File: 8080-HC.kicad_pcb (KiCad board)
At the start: 4 copper layers, 354 parts, among them U1 74HCU04, U10 74HC00, U11 74HC126, U12 74HC161, U13 74HC238, U14 74HC238, U15 74HC238, U16 74HC238, U17 74HC04, U178 74LS03, U18 74HC05, U180 74HC244, U181 74HC244, U182 74HC244, U19 74HC74, U193 74HC244, U194 74HC244, U195 74HC244, U2 74HC74, U20 74HC373, U21 74HC373, U214 74HC373, U215 74HC193, U216 74HC193, U217 74HC193, U218 74HC193, U22 74HC373, U227 74HC04, U228 74HC04, U229 74HC04, U23 74HC373, U230 74HC04, U231 74HC245, U232 74HC04, U233 74HC04, U234 74LS373, U239 74HC74, U24 74HC373, U242 74HC00, U243 74HCU04, U244 74HC00, U25 74HC244, U26 74HC244, U27 74HC244, U28 74HC244, U29 74HC244, U3 74HC00, U30 74HC373, U31 74HC373, U32 74HC244, U33 74HC244, U34 74HC244, U35 74HC244, U36 74HC373, U38 74HC244, U39 74HC244, U4 74HC04, U48 74HC04, U49 74HC04, U5 74HC00, U50 74HC04, U51 74HC04, U52 74HC04, U53 74HC238, U54 74HC238, U55 74HC238, U56 74HC238, U57 74HC04, U58 74HC04, U6 74HC04, U69 74HC05, U7 74HC05, U70 74LS05, U71 74HC04, U72 74LS126, U73 74LS126, U74 74LS126, U75 74LS126, U76 74LS126, U77 74HC00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

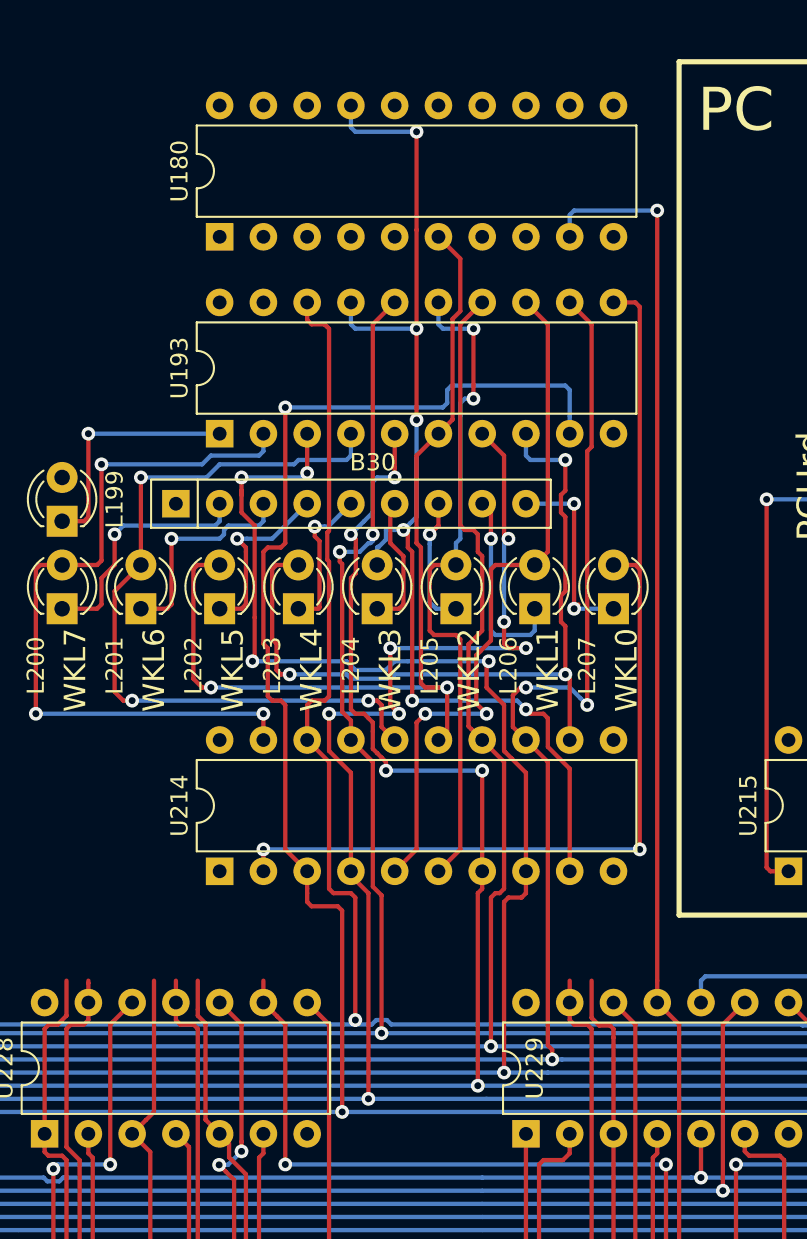
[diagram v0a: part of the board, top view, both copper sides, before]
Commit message: route A0-A3
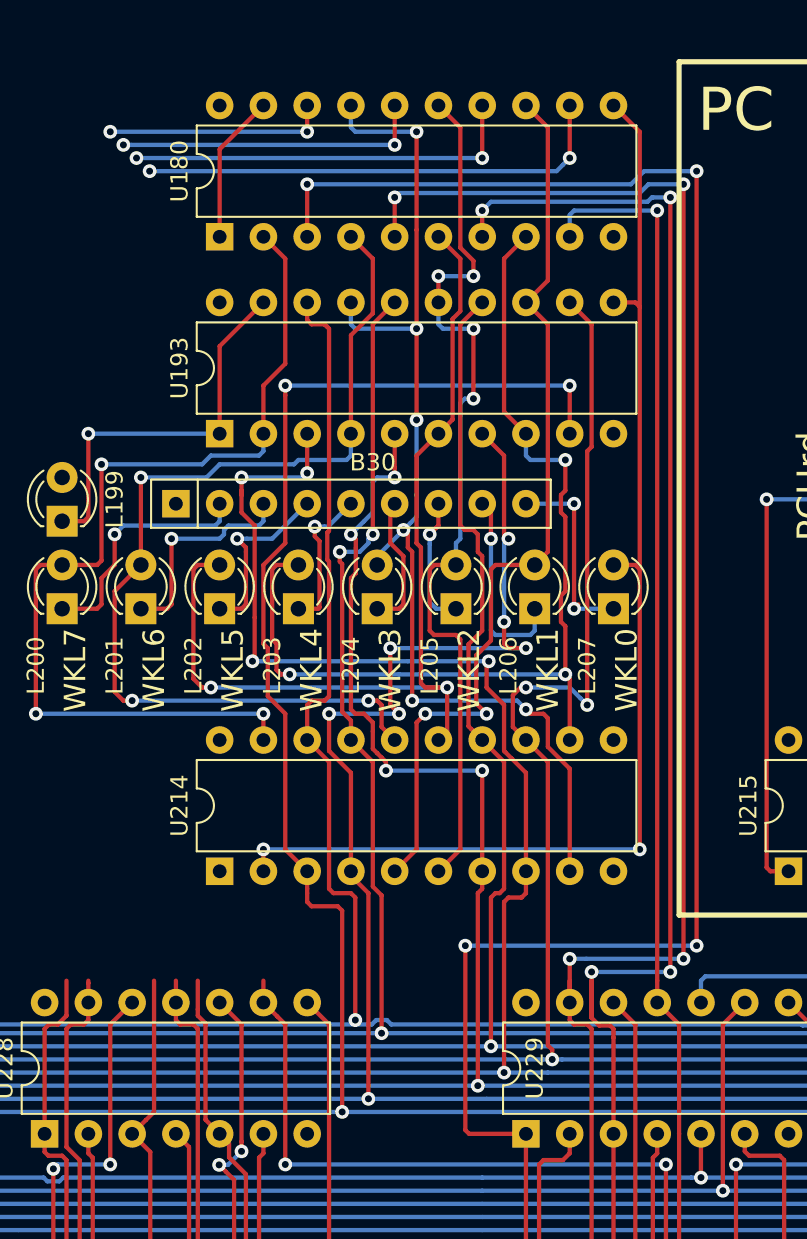
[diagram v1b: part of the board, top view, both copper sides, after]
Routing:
- net A3: track 123.9 -> 222.6 mm, vias 3 -> 7
- net A2: track 132.3 -> 205.7 mm, vias 3 -> 7
- net A1: track 133.2 -> 198.2 mm, vias 3 -> 7
- net A4: track 145.3 -> 173.0 mm, vias 5 -> 7
- net A5: track 92.8 -> 115.9 mm, vias 1 -> 3
- net A6: track 88.9 -> 106.9 mm, vias 1 -> 3
- net Net-(L205-Pad2): track 39.0 -> 53.3 mm, vias 2 -> 4
- net A7: track 85.0 -> 98.0 mm, vias 1 -> 3
- net Net-(L206-Pad2): track 41.4 -> 53.9 mm
- net Net-(L200-Pad2): track 43.5 -> 55.9 mm
- net Net-(L201-Pad2): track 45.2 -> 57.7 mm
- net Net-(L207-Pad2): track 57.9 -> 70.2 mm
- net Net-(L203-Pad2): track 45.1 -> 57.4 mm
- net WKsel: track 0.00 -> 8.67 mm
- net WKLregRD: track 14.1 -> 22.7 mm
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
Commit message: oops, had to redo part of the PC because I inverted U182 and U195, also routed A0-A7 through the PC register
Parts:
- added U43: 74HC04, Package_DIP:DIP-14_W7.62mm, F.Cu at (-367.5, -208.3)
- added U44: 74HC04, Package_DIP:DIP-14_W7.62mm, F.Cu at (-356.7, -208.3)
- added U47: 74HC04, Package_DIP:DIP-14_W7.62mm, F.Cu at (-345.8, -208.3)
- R49, R50, R51, R66: footprint Resistor_THT:R_Axial_DIN0207_L6.3mm_D2.5mm_P10.16mm_Horizontal -> Resistor_THT:R_Axial_DIN0204_L3.6mm_D1.6mm_P5.08mm_Horizontal
- moved R50 133.5 mm to (-311.4, -75.9), turned to 270 degrees
- moved L187 104.4 mm to (-314.8, -97.2)
- moved R49 71.8 mm to (-313.1, -102.9)
- moved L208 56.9 mm to (-279.4, -66.0), turned to 90 degrees
- moved R66 49.8 mm to (-275.3, -85.6), turned to 90 degrees
- moved R51 13.1 mm to (-312.5, -106.2)
- moved U182 11.5 mm to (-221.0, -82.5)
- moved U195 11.5 mm to (-221.0, -71.1)
- moved B5 0.32 mm to (-424.4, -18.7)
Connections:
- B38 pad 2: (no net) -> Net-(B38-Pad2)
- B38 pad 3: (no net) -> Net-(B38-Pad3)
- B38 pad 4: (no net) -> Net-(B38-Pad4)
- B38 pad 5: (no net) -> Net-(B38-Pad5)
- B38 pad 8: (no net) -> Net-(B38-Pad8)
- B38 pad 9: (no net) -> Net-(B38-Pad9)
- L218 pad 1: (no net) -> Net-(L218-Pad1)
- L277 pad 1: (no net) -> BUSAK
- U10 pad 10: (no net) -> Net-(U10-Pad10)
- U10 pad 11: (no net) -> Net-(U10-Pad11)
- U10 pad 12: (no net) -> Net-(U10-Pad12)
- U10 pad 13: (no net) -> Net-(U10-Pad13)
- U10 pad 8: (no net) -> Net-(U10-Pad8)
- U10 pad 9: (no net) -> Net-(U10-Pad9)
- U11 pad 1: (no net) -> Net-(U11-Pad1)
- U11 pad 11: (no net) -> /Timings Generator/QC
- U11 pad 3: (no net) -> /Timings Generator/QA
- U11 pad 6: (no net) -> /Timings Generator/QB
- U11 pad 8: (no net) -> /Timings Generator/QD
- U12 pad 2: (no net) -> /Timings Generator/CLK
- U13 pad 10: (no net) -> Net-(U13-Pad10)
- U13 pad 11: (no net) -> Net-(U13-Pad11)
- U13 pad 12: (no net) -> Net-(U13-Pad12)
- U13 pad 13: (no net) -> /Timings Generator/W2
- U13 pad 14: (no net) -> /Timings Generator/W1
- U13 pad 15: (no net) -> /Timings Generator/W0
- U13 pad 7: (no net) -> Net-(U13-Pad7)
- U13 pad 9: (no net) -> Net-(U13-Pad9)
- U14 pad 10: (no net) -> Net-(U14-Pad10)
- U14 pad 11: (no net) -> Net-(U14-Pad11)
- U14 pad 12: (no net) -> Net-(U14-Pad12)
- U14 pad 13: (no net) -> /Timings Generator/M2
- U14 pad 14: (no net) -> Net-(U14-Pad14)
- U14 pad 15: (no net) -> Net-(U14-Pad15)
- U14 pad 7: (no net) -> Net-(U14-Pad7)
- U14 pad 9: (no net) -> Net-(U14-Pad9)
- U15 pad 10: (no net) -> Net-(U15-Pad10)
- U15 pad 11: (no net) -> /Timings Generator/T12
- U15 pad 12: (no net) -> Net-(U15-Pad12)
- U15 pad 13: (no net) -> /Timings Generator/T10
- U15 pad 14: (no net) -> /Timings Generator/T9
- U15 pad 15: (no net) -> /Timings Generator/T8
- U15 pad 7: (no net) -> Net-(U15-Pad7)
- U15 pad 9: (no net) -> Net-(U15-Pad9)
- U16 pad 10: (no net) -> /Timings Generator/T5
- U16 pad 11: (no net) -> /Timings Generator/T4
- U16 pad 12: (no net) -> /Timings Generator/T3
- U16 pad 13: (no net) -> /Timings Generator/T2
- U16 pad 14: (no net) -> /Timings Generator/T1
- U16 pad 15: (no net) -> /Timings Generator/T0
- U16 pad 7: (no net) -> /Timings Generator/T7
- U16 pad 9: (no net) -> /Timings Generator/T6
- U17 pad 12: (no net) -> Net-(U17-Pad12)
- U17 pad 13: (no net) -> Net-(U17-Pad13)
- U178 pad 4: (no net) -> PCCKdE
- U178 pad 5: (no net) -> T3
- U18 pad 10: (no net) -> Net-(U18-Pad10)
- U18 pad 11: (no net) -> Net-(U18-Pad11)
- U18 pad 12: (no net) -> Net-(U18-Pad12)
- U18 pad 13: (no net) -> Net-(U18-Pad13)
- U18 pad 4: (no net) -> /regs_decode/dataOUT
- U18 pad 8: (no net) -> /regs_decode/memRD
- U181 pad 12: (no net) -> A11
- U181 pad 14: (no net) -> A10
- U181 pad 16: (no net) -> A9
- U181 pad 18: (no net) -> A8
- U181 pad 3: (no net) -> A12
- U181 pad 5: (no net) -> A13
- U181 pad 7: (no net) -> A14
- U181 pad 9: (no net) -> Net-(U181-Pad9)
- U182 pad 12: (no net) -> A3
- U182 pad 14: (no net) -> A2
- U182 pad 16: (no net) -> A1
- U182 pad 18: (no net) -> A0
- U182 pad 3: (no net) -> A4
- U182 pad 5: (no net) -> A5
- U182 pad 7: (no net) -> A6
- U182 pad 9: (no net) -> A7
- U19 pad 10: (no net) -> Net-(U19-Pad10)
- U19 pad 11: (no net) -> Net-(U19-Pad11)
- U19 pad 12: (no net) -> Net-(U19-Pad12)
- U19 pad 13: (no net) -> Net-(U19-Pad13)
- U19 pad 5: (no net) -> Net-(U19-Pad5)
- U19 pad 8: (no net) -> Net-(U19-Pad8)
- U19 pad 9: (no net) -> Net-(U19-Pad9)
- U2 pad 9: (no net) -> Net-(U2-Pad9)
- U20 pad 11: (no net) -> /regs_A_B_C_D_E/AregWR
- U21 pad 11: (no net) -> /regs_A_B_C_D_E/BregWR
- U214 pad 11: (no net) -> WKLregWR
- U215 pad 12: (no net) -> Net-(U215-Pad12)
- U215 pad 13: (no net) -> Net-(U215-Pad13)
- U216 pad 12: (no net) -> Net-(U216-Pad12)
- U217 pad 12: (no net) -> Net-(U217-Pad12)
- U218 pad 12: (no net) -> Net-(U218-Pad12)
- U22 pad 11: (no net) -> /regs_A_B_C_D_E/CregWR
- U23 pad 11: (no net) -> /regs_A_B_C_D_E/DregWR
- U231 pad 1: (no net) -> DataDIR
- U231 pad 19: (no net) -> DataG
- U234 pad 11: (no net) -> /I/O regs/T1
- U24 pad 11: (no net) -> /regs_A_B_C_D_E/EregWR
- U242 pad 8: (no net) -> CLK
- U244 pad 11: (no net) -> CLK2
- U244 pad 3: (no net) -> /I/O control/DataDIR
- U3 pad 10: (no net) -> /HALT/T2
- U3 pad 9: (no net) -> /HALT/HALT
- U30 pad 11: (no net) -> /regs_HL/HregWR
- U31 pad 11: (no net) -> /regs_HL/LregWR
- U32 pad 12: (no net) -> /regs_HL/A12
- U32 pad 14: (no net) -> /regs_HL/A13
- U32 pad 16: (no net) -> /regs_HL/A14
- U32 pad 18: (no net) -> /regs_HL/A15
- U32 pad 3: (no net) -> /regs_HL/A11
- U32 pad 5: (no net) -> /regs_HL/A10
- U32 pad 7: (no net) -> /regs_HL/A9
- U32 pad 9: (no net) -> /regs_HL/A8
- U34 pad 12: (no net) -> /regs_HL/A4
- U34 pad 14: (no net) -> /regs_HL/A5
- U34 pad 16: (no net) -> /regs_HL/A6
- U34 pad 18: (no net) -> /regs_HL/A7
- U34 pad 3: (no net) -> /regs_HL/A3
- U34 pad 5: (no net) -> /regs_HL/A2
- U34 pad 7: (no net) -> /regs_HL/A1
- U34 pad 9: (no net) -> /regs_HL/A0
- U36 pad 11: (no net) -> /reg_WK/WKHregWR
- U38 pad 12: (no net) -> /reg_WK/A12
- U38 pad 14: (no net) -> /reg_WK/A13
- U38 pad 16: (no net) -> /reg_WK/A14
- U38 pad 18: (no net) -> /reg_WK/A15
- U38 pad 3: (no net) -> /reg_WK/A11
- U38 pad 5: (no net) -> /reg_WK/A10
- U38 pad 7: (no net) -> /reg_WK/A9
- U38 pad 9: (no net) -> /reg_WK/A8
- U4 pad 10: (no net) -> Net-(U4-Pad10)
- U4 pad 11: (no net) -> Net-(U4-Pad11)
- U4 pad 12: (no net) -> Net-(U4-Pad12)
- U4 pad 13: (no net) -> Net-(U4-Pad13)
- U4 pad 5: (no net) -> Net-(U4-Pad5)
- U4 pad 6: (no net) -> Net-(U4-Pad6)
- U4 pad 8: (no net) -> Net-(U4-Pad8)
- U4 pad 9: (no net) -> Net-(U4-Pad9)
- U48 pad 10: (no net) -> /regs_decode/PCLregWR
- U48 pad 12: (no net) -> /regs_decode/SPHregWR
- U48 pad 8: (no net) -> /regs_decode/PCHregWR
- U52 pad 1: (no net) -> /regs_decode/T0
- U53 pad 10: (no net) -> /regs_decode/LregWR
- U53 pad 11: (no net) -> /regs_decode/HregWR
- U53 pad 12: (no net) -> /regs_decode/EregWR
- U53 pad 13: (no net) -> /regs_decode/DregWR
- U53 pad 14: (no net) -> /regs_decode/CregWR
- U53 pad 15: (no net) -> /regs_decode/BregWR
- U53 pad 7: (no net) -> /regs_decode/AregWR
- U54 pad 14: (no net) -> /regs_decode/FregWR
- U54 pad 15: (no net) -> Net-(U54-Pad15)
- U54 pad 7: (no net) -> /regs_decode/WKLregWR
- U54 pad 9: (no net) -> /regs_decode/WKHregWR
- U55 pad 10: (no net) -> /regs_decode/LregRD
- U55 pad 11: (no net) -> /regs_decode/HregRD
- U55 pad 12: (no net) -> /regs_decode/EregRD
- U55 pad 13: (no net) -> /regs_decode/DregRD
- U55 pad 14: (no net) -> /regs_decode/CregRD
- U55 pad 15: (no net) -> /regs_decode/BregRD
- U55 pad 7: (no net) -> /regs_decode/AregRD
- U56 pad 10: (no net) -> /regs_decode/SPLregRD
- U56 pad 11: (no net) -> /regs_decode/SPHregRD
- U56 pad 12: (no net) -> /regs_decode/PCLregRD
- U56 pad 13: (no net) -> /regs_decode/PCHregRD
- U56 pad 14: (no net) -> /regs_decode/FregRD
- U56 pad 15: (no net) -> Net-(U56-Pad15)
- U56 pad 7: (no net) -> /regs_decode/WKLregRD
- U56 pad 9: (no net) -> /regs_decode/WKHregRD
- U57 pad 2: (no net) -> /regs_decode/SPLregWR
- U58 pad 3: (no net) -> /regs_decode/Qa
- U6 pad 14: (no net) -> Net-(U6-Pad14)
- U6 pad 4: (no net) -> /Reset/reset(inner)
- U6 pad 7: (no net) -> Net-(U6-Pad7)
- U69 pad 1: (no net) -> /I/O control/W0
- U69 pad 8: (no net) -> /MOV / MVI/s3
- U7 pad 10: (no net) -> /Reset/INTclr
- U7 pad 2: (no net) -> /Reset/OUTdE
- U7 pad 6: (no net) -> /Reset/HLTclr
- U7 pad 8: (no net) -> /Reset/IEFclr
- U77 pad 3: (no net) -> /I/O control/DataG
- U78 pad 3: (no net) -> /I/O control/PCADout
- U79 pad 1: (no net) -> /MOV / MVI/OP7
- U8 pad 1: (no net) -> /BUSRQ/T3
- U80 pad 11: (no net) -> /MOV / MVI/PCsel
- U82 pad 8: (no net) -> /MOV / MVI/HALT
- U83 pad 10: (no net) -> /MOV / MVI/T8
- U83 pad 11: (no net) -> /MOV / MVI/d3
- U83 pad 5: (no net) -> /MOV / MVI/T5
- U83 pad 6: (no net) -> /MOV / MVI/PCinc
- U84 pad 11: (no net) -> /HALT/MCLR
- U84 pad 13: (no net) -> /HALT/T4
- U84 pad 5: (no net) -> /MOV / MVI/M3
- U85 pad 4: (no net) -> /MOV / MVI/HLTA
- U87 pad 11: (no net) -> /MOV / MVI/s2
- U87 pad 3: (no net) -> /MOV / MVI/d2
- U87 pad 6: (no net) -> /MOV / MVI/d1
- U87 pad 8: (no net) -> /MOV / MVI/d0
- U88 pad 3: (no net) -> /MOV / MVI/s1
- U88 pad 6: (no net) -> /MOV / MVI/s0
- U89 pad 8: (no net) -> /INR / DCR decode/LXI
- U9 pad 2: (no net) -> /BUSRQ/Mstop
- U9 pad 4: (no net) -> /BUSRQ/OUTdE
- U91 pad 2: (no net) -> /HALT/HLTclr
- U92 pad 1: (no net) -> /INR / DCR decode/OP0
- U92 pad 10: (no net) -> /INR / DCR decode/DCR
- U92 pad 11: (no net) -> /INR / DCR decode/INR
- U92 pad 12: (no net) -> /INR / DCR decode/INX-DCX
- U92 pad 13: (no net) -> Net-(U92-Pad13)
- U92 pad 15: (no net) -> Net-(U92-Pad15)
- U92 pad 2: (no net) -> /INR / DCR decode/OP1
- U92 pad 3: (no net) -> /INR / DCR decode/OP2
- U92 pad 4: (no net) -> /INR / DCR decode/OP6
- U92 pad 5: (no net) -> /INR / DCR decode/OP7
- U92 pad 7: (no net) -> Net-(U92-Pad7)
- U92 pad 9: (no net) -> Net-(U92-Pad9)
- U93 pad 1: (no net) -> /INR / DCR decode/OP3
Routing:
- net A7: track 98.0 -> 256.6 mm, vias 3 -> 6
- net A6: track 106.9 -> 259.2 mm, vias 3 -> 6
- net A5: track 115.9 -> 255.0 mm, vias 3 -> 8
- net A4: track 173.0 -> 299.9 mm, vias 7 -> 12
- net A3: track 222.6 -> 300.6 mm, vias 7 -> 8
- net A2: track 205.7 -> 280.7 mm, vias 7 -> 8
- net A1: track 198.2 -> 269.1 mm, vias 7 -> 8
- net A0: track 182.4 -> 249.1 mm, vias 4 -> 5
- net iB6: track 388.7 -> 345.4 mm, vias 15 -> 14
- net iB1: track 378.2 -> 340.3 mm
- net iB0: track 384.5 -> 352.1 mm, vias 12 -> 11
- net WKLregWR: track 0.00 -> 25.9 mm, vias 0 -> 2
- net iB5: track 373.2 -> 352.6 mm, vias 9 -> 7
- net iB7: track 354.9 -> 337.1 mm, vias 8 -> 9
- net Net-(L208-Pad1): track 0.00 -> 15.9 mm, vias 0 -> 2
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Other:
- board text added: "WKL"
- board text added: "WKLrd"
- board text added: "WKLwr"

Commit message: fix a couple missing traces
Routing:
- net Net-(L208-Pad1): track 15.9 -> 28.7 mm, vias 2 -> 3
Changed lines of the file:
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@@
     (thickness 1.6)
     (drawings 100)
-    (tracks 2721)
+    (tracks 2726)
     (zones 0)
     (modules 357)
@@
     (descr "20-lead though-hole mounted DIP package, row spacing 7.62 mm (300 mils)")
     (tags "THT DIP DIL PDIP 2.54mm 7.62mm 300mil")
-    (fp_text reference U182 (at 9.271 1.016 180) (layer F.SilkS)
+    (fp_text reference U182 (at 3.81 -2.286 270) (layer F.SilkS)
       (effects (font (size 1 1) (thickness 0.15)))
     )
@@
   (segment (start -280.67 -78.232) (end -279.908 -77.47) (width 0.25) (layer F.Cu) (net 498))
   (via (at -280.67 -80.518) (size 0.8) (drill 0.4) (layers F.Cu B.Cu) (net 498))
+  (via (at -274.066 -80.518) (size 0.8) (drill 0.4) (layers F.Cu B.Cu) (net 498))
+  (segment (start -280.67 -80.518) (end -274.066 -80.518) (width 0.25) (layer B.Cu) (net 498))
+  (segment (start -274.066 -80.518) (end -274.066 -85.344) (width 0.25) (layer F.Cu) (net 498))
+  (segment (start -274.066 -85.344) (end -274.32 -85.598) (width 0.25) (layer F.Cu) (net 498))
+  (segment (start -274.32 -85.598) (end -275.336 -85.598) (width 0.25) (layer F.Cu) (net 498))
   (zone (net 3) (net_name VCC) (layer VCC) (hatch edge 0.508)
     (connect_pads (clearance 0.508))

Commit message: route part of A8-A15 from WKL to WKH
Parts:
- removed D83: LED_Small_ALT, LED_THT:LED_D3.0mm
- removed U36: 74HC373, Package_DIP:DIP-20_W7.62mm
- added L190: LED_Small_ALT, LED_THT:LED_D3.0mm, F.Cu at (-355.0, -61.0)
- added L198: LED_Small_ALT, LED_THT:LED_D3.0mm, F.Cu at (-322.8, -66.0)
- added R65: 1K, Resistor_THT:R_Axial_DIN0204_L3.6mm_D1.6mm_P5.08mm_Horizontal, F.Cu at (-318.0, -66.0)
- added U213: 74HC373, Package_DIP:DIP-20_W7.62mm, F.Cu at (-345.4, -45.7)
- B29: renamed from RN8; value R_Network08 -> 2.2K
- R4, R5, R6, R7: footprint Resistor_THT:R_Axial_DIN0207_L6.3mm_D2.5mm_P10.16mm_Horizontal -> Resistor_THT:R_Axial_DIN0204_L3.6mm_D1.6mm_P5.08mm_Horizontal
- R64: renamed from R18; value R -> 1K; footprint Resistor_THT:R_Axial_DIN0207_L6.3mm_D2.5mm_P10.16mm_Horizontal -> Resistor_THT:R_Axial_DIN0204_L3.6mm_D1.6mm_P5.08mm_Horizontal
- moved L189 516.7 mm to (-355.0, -66.0), turned to 90 degrees
- moved L191 504.5 mm to (-350.3, -61.0), turned to 90 degrees
- moved L194 476.6 mm to (-336.6, -61.0), turned to 90 degrees
- moved L192 471.8 mm to (-345.7, -61.0), turned to 90 degrees
- moved U192 464.2 mm to (-345.4, -71.1), turned to 90 degrees
- moved L193 457.6 mm to (-341.1, -61.0), turned to 90 degrees
- moved L195 457.2 mm to (-332.0, -61.0), turned to 90 degrees
- moved L197 449.6 mm to (-322.8, -61.0), turned to 90 degrees
- moved U179 448.8 mm to (-345.4, -82.5), turned to 90 degrees
- moved L196 443.0 mm to (-327.4, -61.0), turned to 90 degrees
- moved R64 430.7 mm to (-355.0, -75.9), turned to 270 degrees
- moved B29 419.4 mm to (-328.2, -67.1), turned to 180 degrees
- moved R51 52.1 mm to (-266.2, -82.3)
- moved R49 24.9 mm to (-311.4, -78.0), turned to 90 degrees
- moved D85 21.0 mm to (48.8, -284.5)
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- renumbered D86 to L189, D81 to L191, D79 to L192, D77 to L193, D75 to L194, D73 to L195, D71 to L196, D69 to L197, U38 to U179, U39 to U192
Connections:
- U179 pad 12: /reg_WK/A12 -> A12
- U179 pad 14: /reg_WK/A13 -> A13
- U179 pad 16: /reg_WK/A14 -> A14
- U179 pad 18: /reg_WK/A15 -> A15
- U179 pad 3: /reg_WK/A11 -> A11
- U179 pad 5: /reg_WK/A10 -> A10
- U179 pad 7: /reg_WK/A9 -> A9
- U179 pad 9: /reg_WK/A8 -> A8
- U181 pad 9: Net-(U181-Pad9) -> A15
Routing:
- net A15: track 38.0 -> 169.3 mm, vias 1 -> 4
- net A11: track 50.1 -> 159.0 mm, vias 3 -> 8
- net A14: track 50.4 -> 147.4 mm, vias 1 -> 4
- net A10: track 64.7 -> 156.9 mm, vias 1 -> 5
- net A13: track 49.1 -> 140.8 mm, vias 1 -> 6
- net A12: track 57.8 -> 147.3 mm, vias 1 -> 6
- net A9: track 79.5 -> 165.7 mm, vias 1 -> 5
- net A8: track 80.7 -> 161.3 mm, vias 1 -> 5
- net WKsel: track 8.67 -> 65.0 mm, vias 0 -> 2
- net iB0: track 352.1 -> 376.4 mm
- net Net-(L187-Pad2): track 0.00 -> 4.83 mm
- net Net-(L205-Pad2): track 53.3 -> 56.9 mm
- net A6: track 259.2 -> 260.3 mm
- net A7: track 256.6 -> 257.4 mm
- net A4: track 299.9 -> 299.4 mm
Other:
- board text added: "WKsel"

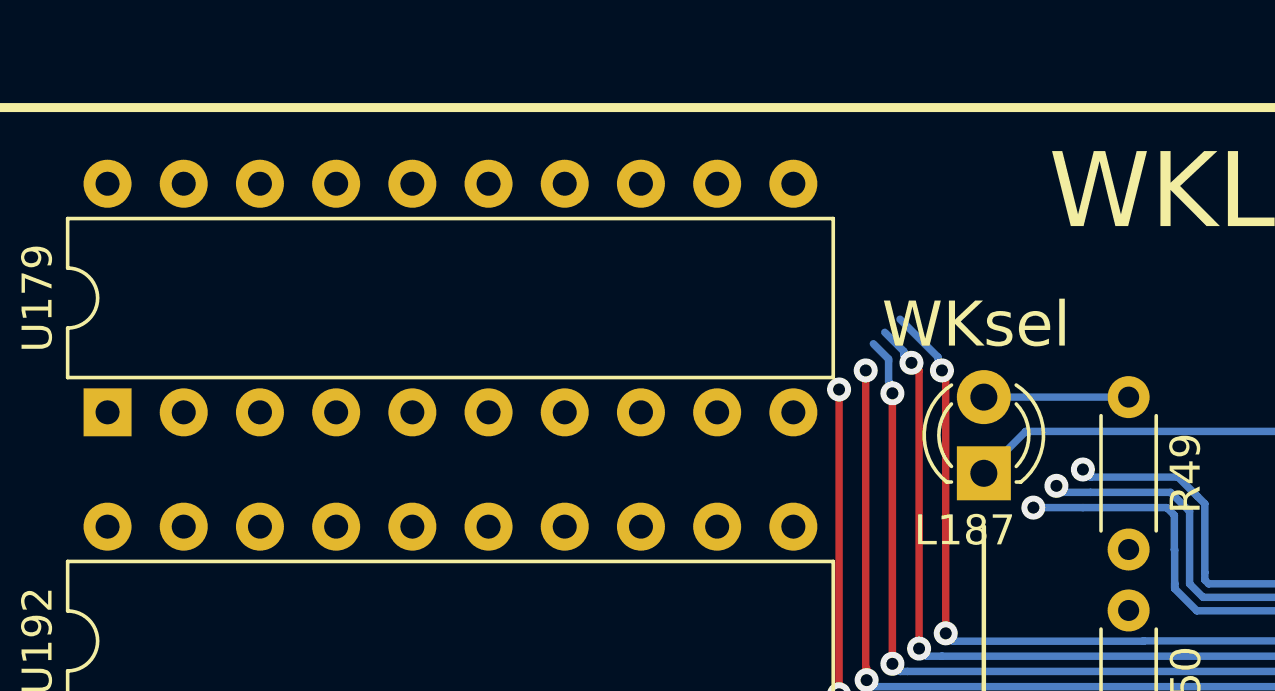
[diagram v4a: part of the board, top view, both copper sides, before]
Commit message: finish routing A8-A15 from WKL to WKH
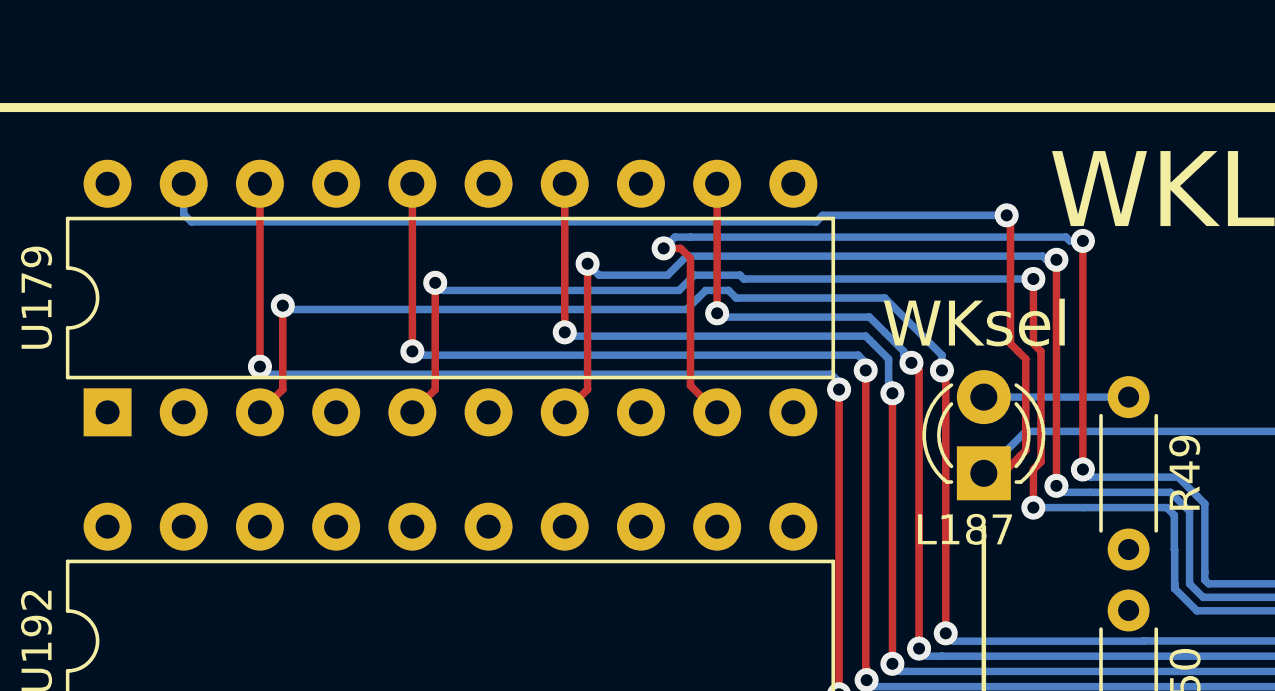
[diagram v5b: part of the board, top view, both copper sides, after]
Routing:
- net WKsel: track 65.0 -> 103.4 mm, vias 2 -> 3
- net A10: track 156.9 -> 189.6 mm, vias 5 -> 7
- net A9: track 165.7 -> 194.6 mm, vias 5 -> 7
- net A8: track 161.3 -> 189.7 mm, vias 5 -> 7
- net A15: track 169.3 -> 195.1 mm, vias 4 -> 5
- net A11: track 159.0 -> 184.5 mm, vias 8 -> 9
- net A14: track 147.4 -> 168.5 mm, vias 4 -> 5
- net A13: track 140.8 -> 156.2 mm, vias 6 -> 7
- net A12: track 147.3 -> 157.4 mm, vias 6 -> 7
